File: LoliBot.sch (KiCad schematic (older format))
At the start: 25 parts, among them J1 LOLINBATT, J2 APA106, J3 SERVO1, J4 RIGHT, J5 LEFT, J6 MPU-9250, J7 APA106, SW1 SPST, U1 LOLIN32-LITE, U2 RT9276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

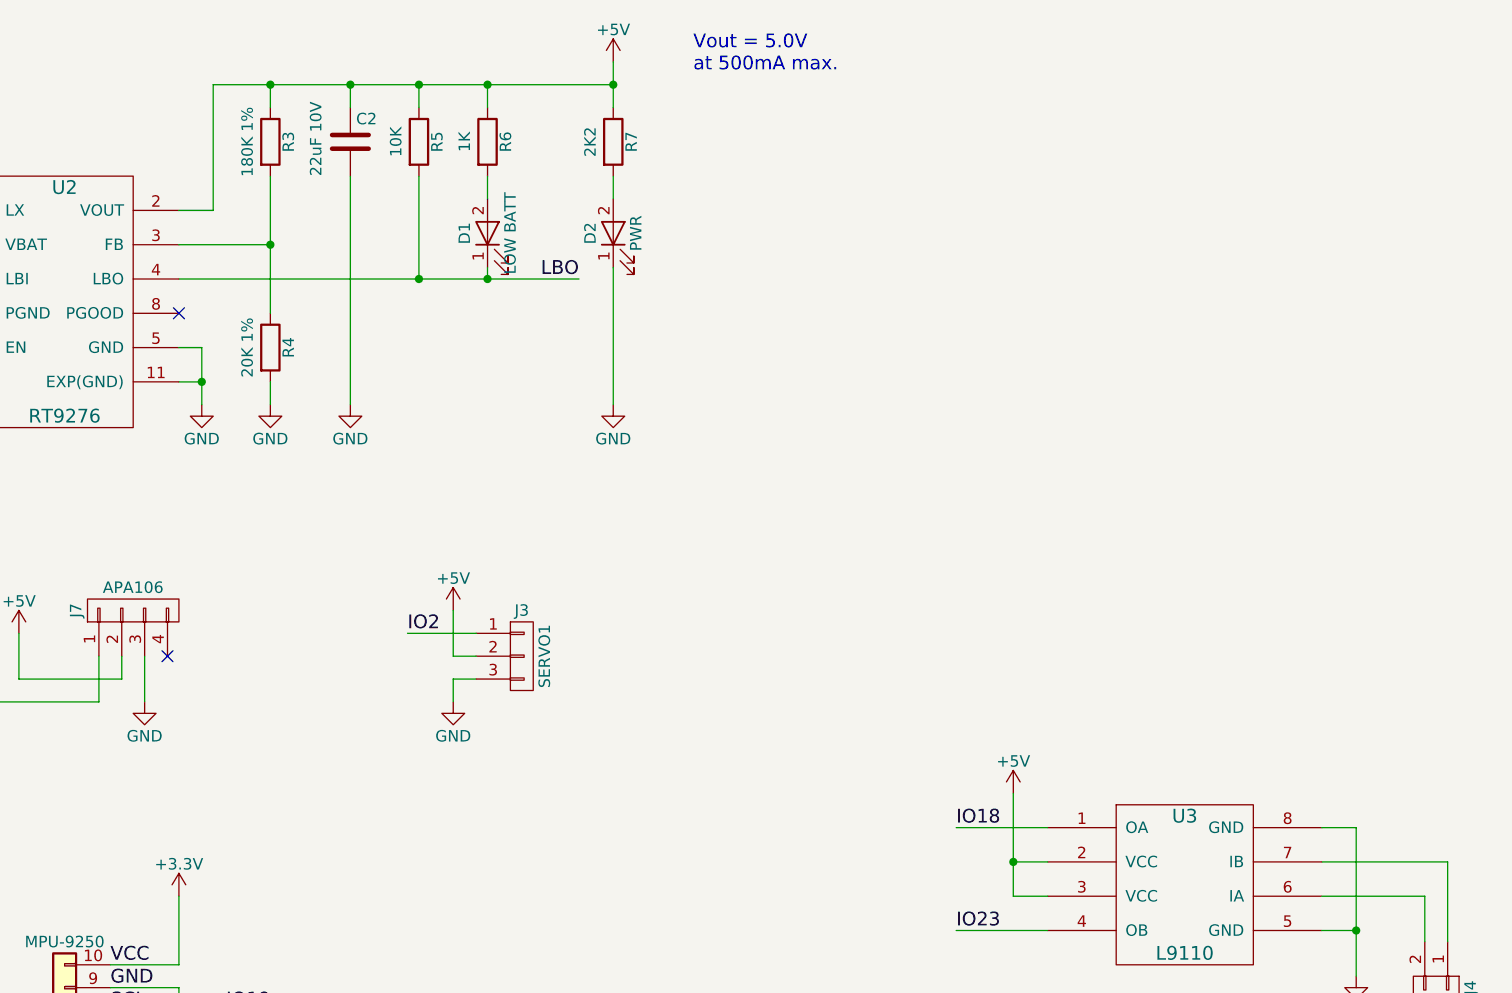
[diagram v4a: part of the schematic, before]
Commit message: Added Board for JS Version
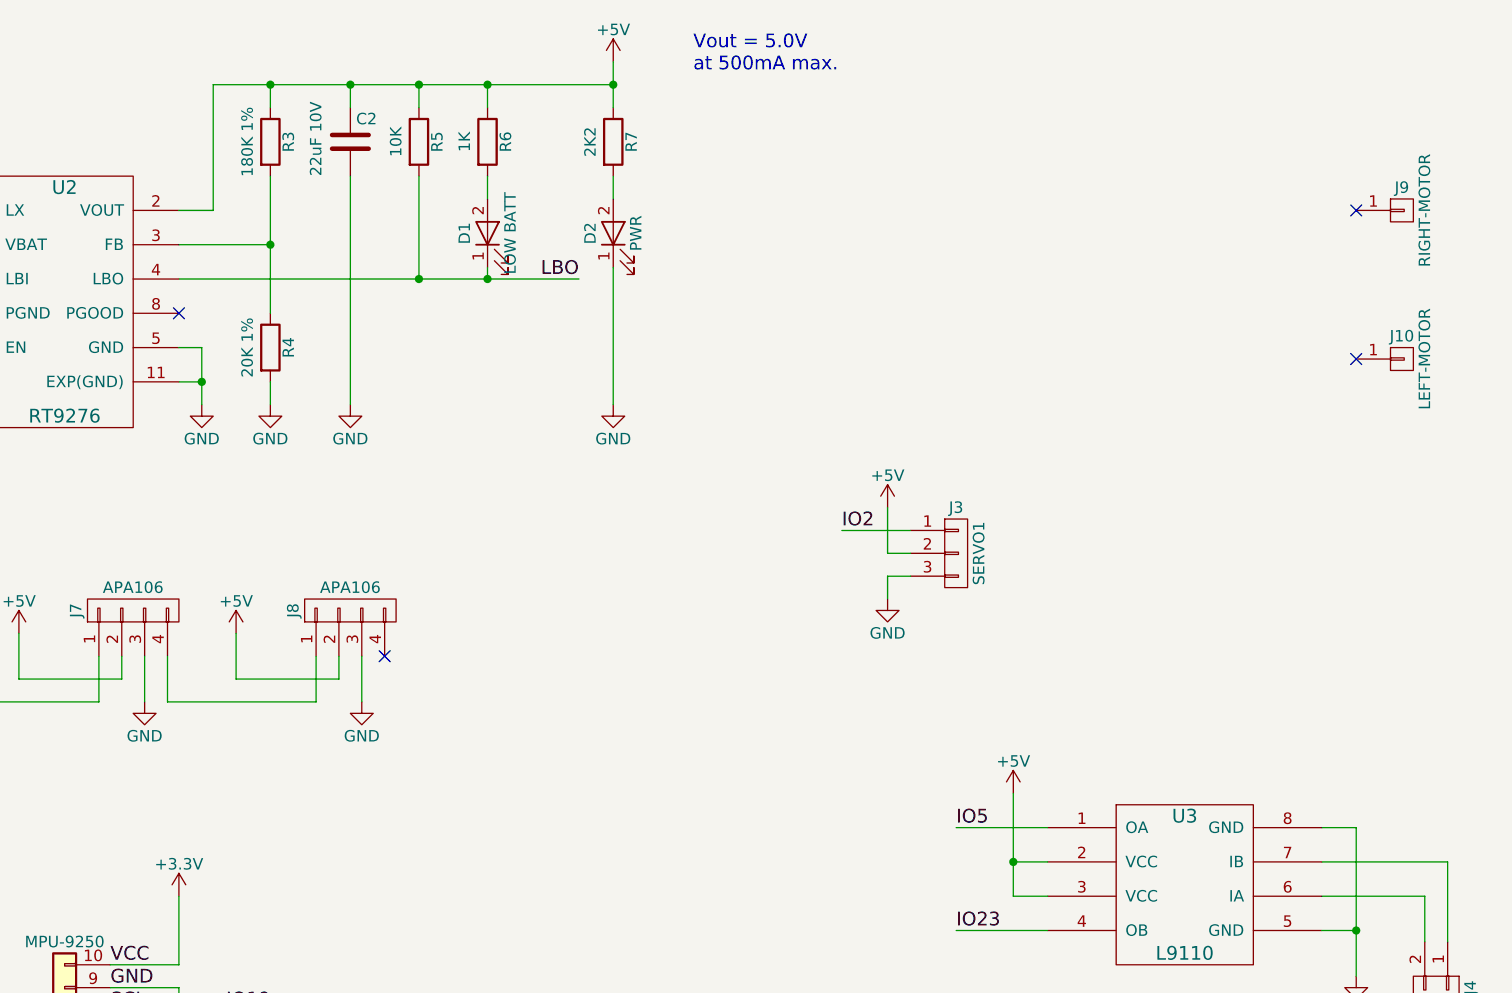
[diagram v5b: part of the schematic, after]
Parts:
- added J10: LEFT-MOTOR, libs:DC-Motor, symbol CONN_01X01
- added J8: APA106, libs:LED_8MM_APA-106, symbol CONN_01X04
- added J9: RIGHT-MOTOR, libs:DC-Motor, symbol CONN_01X01
- BT1: footprint (none) -> libs:BH-18650
- C1, C2: footprint (none) -> Capacitors_SMD:C_1210_HandSoldering
- D1, D2: footprint (none) -> LEDs:LED_D3.0mm
- J1: footprint (none) -> Pin_Headers:Pin_Header_Straight_1x02_Pitch2.54mm
- J2, J7: footprint (none) -> libs:LED_8MM_APA-106
- J3: footprint (none) -> Pin_Headers:Pin_Header_Straight_1x03_Pitch2.54mm
- J4, J5: footprint Connectors_JST:JST_PH_B2B-PH-K_02x2.00mm_Straight -> Pin_Headers:Pin_Header_Straight_1x02_Pitch2.00mm
- J6: footprint (none) -> Pin_Headers:Pin_Header_Straight_1x10_Pitch2.54mm
- R1, R2, R3, R4, R5, R6, R7: footprint (none) -> Resistors_SMD:R_0805_HandSoldering
- SW1: footprint (none) -> libs:SS12D00
- U1: footprint (none) -> libs:lolin32-lite
- U3, U4: footprint (none) -> Housings_DIP:DIP-8_W7.62mm
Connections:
- net +5V: now also J8.2 (P2)
- net GND: now also J8.3 (P3)
- net IO18: no longer U3.1 (OA)
- net IO5: now also U3.1 (OA)
- net at J7.4 (P4): now also J8.1 (P1)
- no-connect marks 7 -> 9
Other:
- moved on the sheet: J3

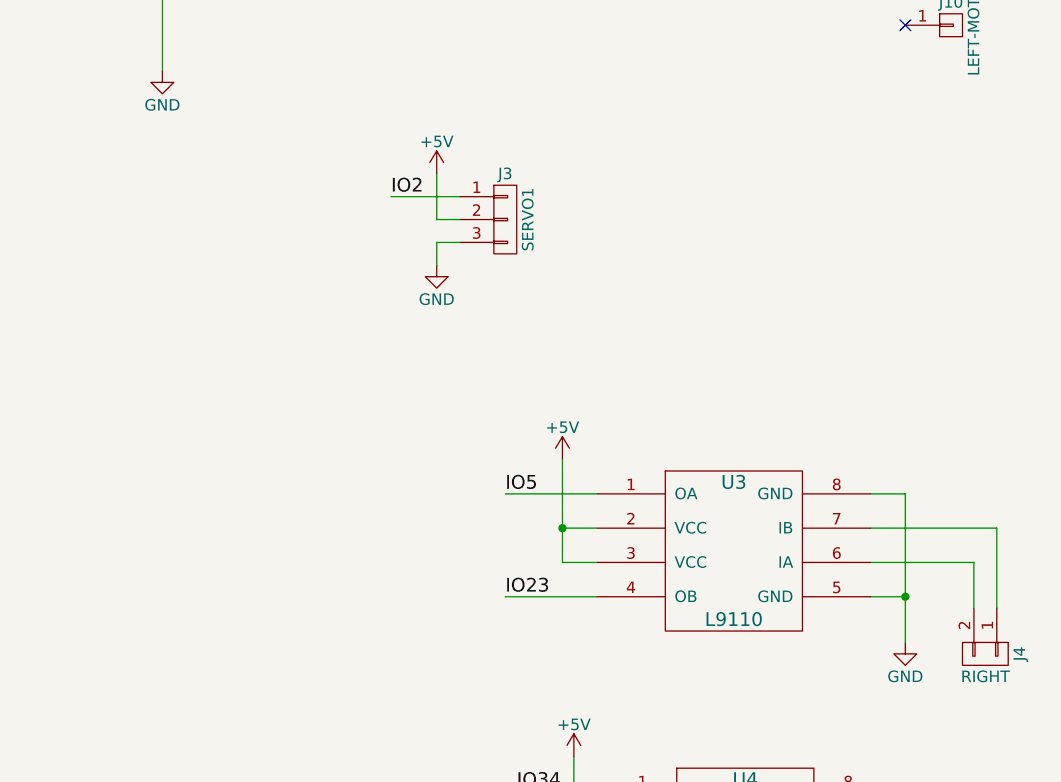
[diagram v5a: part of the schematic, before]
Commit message: Added Mounting brackets and IR sensor
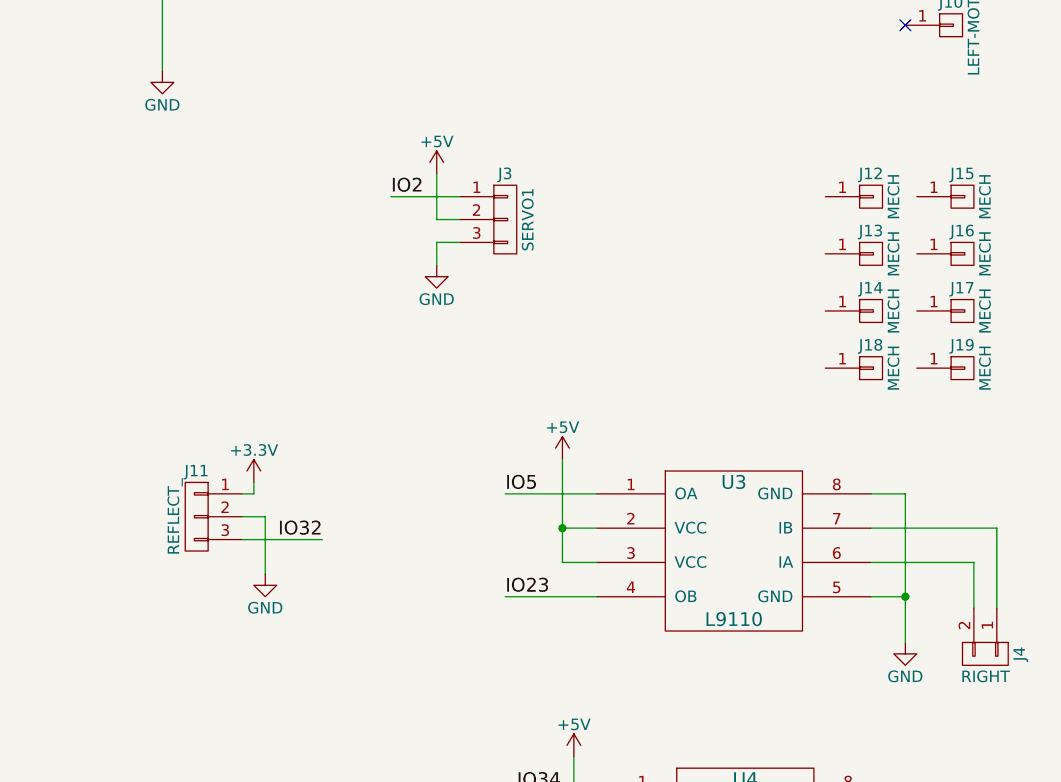
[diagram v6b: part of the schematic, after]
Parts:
- added J11: REFLECT_, Pin_Headers:Pin_Header_Straight_1x03_Pitch2.54mm, symbol CONN_01X03
- added J12, J13, J14, J15, J16, J17, J18, J19: MECH, Mounting_Holes:MountingHole_3.2mm_M3_Pad, symbol CONN_01X01
- L1: footprint (none) -> Choke_SMD:Choke_SMD_7.3x7.3_H3.5
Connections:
- net +3V3: now also J11.1 (P1)
- net GND: now also J11.2 (P2)
- net IO32: now also J11.3 (P3)
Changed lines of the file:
@@
 $EndComp
 $Comp
-L GND #PWR1
+L GND #PWR01
 U 1 1 59DB6136
 P 1250 2150
-F 0 "#PWR1" H 1250 1900 50  0001 C CNN
+F 0 "#PWR01" H 1250 1900 50  0001 C CNN
 F 1 "GND" H 1250 2000 50  0000 C CNN
 F 2 "" H 1250 2150 50  0001 C CNN
@@
 F 0 "L1" V 3350 1000 50  0000 C CNN
 F 1 "7.4uH CDRH" V 3475 1000 50  0000 C CNN
-F 2 "" H 3400 1000 50  0001 C CNN
+F 2 "Choke_SMD:Choke_SMD_7.3x7.3_H3.5" H 3400 1000 50  0001 C CNN
 F 3 "" H 3400 1000 50  0001 C CNN
 	1    3400 1000
@@
 $EndComp
 $Comp
-L GND #PWR3
+L GND #PWR02
 U 1 1 59DB694D
 P 2900 1800
-F 0 "#PWR3" H 2900 1550 50  0001 C CNN
+F 0 "#PWR02" H 2900 1550 50  0001 C CNN
 F 1 "GND" H 2900 1650 50  0000 C CNN
 F 2 "" H 2900 1800 50  0001 C CNN
@@
 	3300 2100 3300 2200
 $Comp
-L GND #PWR4
+L GND #PWR03
 U 1 1 59DB6ABB
 P 3300 2200
-F 0 "#PWR4" H 3300 1950 50  0001 C CNN
+F 0 "#PWR03" H 3300 1950 50  0001 C CNN
 F 1 "GND" H 3300 2050 50  0000 C CNN
 F 2 "" H 3300 2200 50  0001 C CNN
@@
 NoConn ~ 5300 1850
 $Comp
-L GND #PWR13
+L GND #PWR04
 U 1 1 59DB708D
 P 5400 2250
-F 0 "#PWR13" H 5400 2000 50  0001 C CNN
+F 0 "#PWR04" H 5400 2000 50  0001 C CNN
 F 1 "GND" H 5400 2100 50  0000 C CNN
 F 2 "" H 5400 2250 50  0001 C CNN
@@
 $EndComp
 $Comp
-L GND #PWR7
+L GND #PWR05
 U 1 1 59DB70B0
 P 4150 2150
-F 0 "#PWR7" H 4150 1900 50  0001 C CNN
+F 0 "#PWR05" H 4150 1900 50  0001 C CNN
 F 1 "GND" H 4150 2000 50  0000 C CNN
 F 2 "" H 4150 2150 50  0001 C CNN
@@
 Connection ~ 5700 1550
 $Comp
-L GND #PWR15
+L GND #PWR06
 U 1 1 59DB7D00
 P 5700 2250
-F 0 "#PWR15" H 5700 2000 50  0001 C CNN
+F 0 "#PWR06" H 5700 2000 50  0001 C CNN
 F 1 "GND" H 5700 2100 50  0000 C CNN
 F 2 "" H 5700 2250 50  0001 C CNN
@@
 	6050 1250 6050 2250
 $Comp
-L GND #PWR16
+L GND #PWR07
 U 1 1 59DB7E46
 P 6050 2250
-F 0 "#PWR16" H 6050 2000 50  0001 C CNN
+F 0 "#PWR07" H 6050 2000 50  0001 C CNN
 F 1 "GND" H 6050 2100 50  0000 C CNN
 F 2 "" H 6050 2250 50  0001 C CNN
@@
 $EndComp
 $Comp
-L GND #PWR19
+L GND #PWR08
 U 1 1 59DB834E
 P 7200 2250
-F 0 "#PWR19" H 7200 2000 50  0001 C CNN
+F 0 "#PWR08" H 7200 2000 50  0001 C CNN
 F 1 "GND" H 7200 2100 50  0000 C CNN
 F 2 "" H 7200 2250 50  0001 C CNN
@@
 	7200 1650 7200 2250
 $Comp
-L +5V #PWR18
+L +5V #PWR09
 U 1 1 59DB92E1
 P 7200 750
-F 0 "#PWR18" H 7200 600 50  0001 C CNN
+F 0 "#PWR09" H 7200 600 50  0001 C CNN
 F 1 "+5V" H 7200 890 50  0000 C CNN
 F 2 "" H 7200 750 50  0001 C CNN
@@
 $EndComp
 $Comp
-L +5V #PWR6
+L +5V #PWR010
 U 1 1 59DBA2B8
 P 3750 3250
-F 0 "#PWR6" H 3750 3100 50  0001 C CNN
+F 0 "#PWR010" H 3750 3100 50  0001 C CNN
 F 1 "+5V" H 3750 3390 50  0000 C CNN
 F 2 "" H 3750 3250 50  0001 C CNN
@@
 $EndComp
 $Comp
-L GND #PWR8
+L GND #PWR011
 U 1 1 59DBA675
 P 4300 3550
-F 0 "#PWR8" H 4300 3300 50  0001 C CNN
+F 0 "#PWR011" H 4300 3300 50  0001 C CNN
 F 1 "GND" H 4300 3400 50  0000 C CNN
 F 2 "" H 4300 3550 50  0001 C CNN
@@
 $EndComp
 $Comp
-L GND #PWR24
+L GND #PWR012
 U 1 1 59DBB61B
 P 10450 4750
-F 0 "#PWR24" H 10450 4500 50  0001 C CNN
+F 0 "#PWR012" H 10450 4500 50  0001 C CNN
 F 1 "GND" H 10450 4600 50  0000 C CNN
 F 2 "" H 10450 4750 50  0001 C CNN
@@
 	10850 4250 10850 4600
 $Comp
-L +5V #PWR22
+L +5V #PWR013
 U 1 1 59DBBC2C
 P 8950 3950
-F 0 "#PWR22" H 8950 3800 50  0001 C CNN
+F 0 "#PWR013" H 8950 3800 50  0001 C CNN
 F 1 "+5V" H 8950 4090 50  0000 C CNN
 F 2 "" H 8950 3950 50  0001 C CNN
@@
 $EndComp
 $Comp
-L GND #PWR25
+L GND #PWR014
 U 1 1 59DBCDC3
 P 10500 6050
-F 0 "#PWR25" H 10500 5800 50  0001 C CNN
+F 0 "#PWR014" H 10500 5800 50  0001 C CNN
 F 1 "GND" H 10500 5900 50  0000 C CNN
 F 2 "" H 10500 6050 50  0001 C CNN
@@
 	10900 5550 10900 5900
 $Comp
-L +5V #PWR23
+L +5V #PWR015
 U 1 1 59DBCDD1
 P 9000 5250
-F 0 "#PWR23" H 9000 5100 50  0001 C CNN
+F 0 "#PWR015" H 9000 5100 50  0001 C CNN
 F 1 "+5V" H 9000 5390 50  0000 C CNN
 F 2 "" H 9000 5250 50  0001 C CNN
@@
 $EndComp
 $Comp
-L +5V #PWR20
+L +5V #PWR016
 U 1 1 59DBDAEB
 P 8400 2700
-F 0 "#PWR20" H 8400 2550 50  0001 C CNN
+F 0 "#PWR016" H 8400 2550 50  0001 C CNN
 F 1 "+5V" H 8400 2840 50  0000 C CNN
 F 2 "" H 8400 2700 50  0001 C CNN
@@
 $EndComp
 $Comp
-L GND #PWR21
+L GND #PWR017
 U 1 1 59DBDB38
 P 8400 3100
-F 0 "#PWR21" H 8400 2850 50  0001 C CNN
+F 0 "#PWR017" H 8400 2850 50  0001 C CNN
 F 1 "GND" H 8400 2950 50  0000 C CNN
 F 2 "" H 8400 3100 50  0001 C CNN
@@
 IO13
 $Comp
-L +3.3V #PWR5
+L +3.3V #PWR018
 U 1 1 59DC0699
 P 3300 4450
-F 0 "#PWR5" H 3300 4300 50  0001 C CNN
+F 0 "#PWR018" H 3300 4300 50  0001 C CNN
 F 1 "+3.3V" H 3300 4590 50  0000 C CNN
 F 2 "" H 3300 4450 50  0001 C CNN
@@
 $EndComp
 $Comp
-L GND #PWR2
+L GND #PWR019
 U 1 1 59DC0B2B
 P 1300 6000
-F 0 "#PWR2" H 1300 5750 50  0001 C CNN
+F 0 "#PWR019" H 1300 5750 50  0001 C CNN
 F 1 "GND" H 1300 5850 50  0000 C CNN
 F 2 "" H 1300 6000 50  0001 C CNN
@@
 FSYNC
 $Comp
-L +3.3V #PWR11
+L +3.3V #PWR020
 U 1 1 59E28F97
 P 5300 4400
-F 0 "#PWR11" H 5300 4250 50  0001 C CNN
+F 0 "#PWR020" H 5300 4250 50  0001 C CNN
 F 1 "+3.3V" H 5300 4540 50  0000 C CNN
 F 2 "" H 5300 4400 50  0001 C CNN
@@
 	5300 4700 5300 4400
 $Comp
-L GND #PWR12
+L GND #PWR021
 U 1 1 59E29073
 P 5300 5700
-F 0 "#PWR12" H 5300 5450 50  0001 C CNN
+F 0 "#PWR021" H 5300 5450 50  0001 C CNN
 F 1 "GND" H 5300 5550 50  0000 C CNN
 F 2 "" H 5300 5700 50  0001 C CNN
@@
 IO17
 $Comp
-L +5V #PWR9
+L +5V #PWR022
 U 1 1 59E30CAE
 P 4600 3250
-F 0 "#PWR9" H 4600 3100 50  0001 C CNN
+F 0 "#PWR022" H 4600 3100 50  0001 C CNN
 F 1 "+5V" H 4600 3390 50  0000 C CNN
 F 2 "" H 4600 3250 50  0001 C CNN
@@
 	5150 3350 5150 3550
 $Comp
-L GND #PWR10
+L GND #PWR023
 U 1 1 59E30F3C
 P 5150 3550
-F 0 "#PWR10" H 5150 3300 50  0001 C CNN
+F 0 "#PWR023" H 5150 3300 50  0001 C CNN
 F 1 "GND" H 5150 3400 50  0000 C CNN
 F 2 "" H 5150 3550 50  0001 C CNN
@@
 	5900 3550 5900 3350
 $Comp
-L +5V #PWR14
+L +5V #PWR024
 U 1 1 59F090B9
 P 5550 3250
-F 0 "#PWR14" H 5550 3100 50  0001 C CNN
+F 0 "#PWR024" H 5550 3100 50  0001 C CNN
 F 1 "+5V" H 5550 3390 50  0000 C CNN
 F 2 "" H 5550 3250 50  0001 C CNN
@@
 	6100 3350 6100 3550
 $Comp
-L GND #PWR17
+L GND #PWR025
 U 1 1 59F090C3
 P 6100 3550
-F 0 "#PWR17" H 6100 3300 50  0001 C CNN
+F 0 "#PWR025" H 6100 3300 50  0001 C CNN
 F 1 "GND" H 6100 3400 50  0000 C CNN
 F 2 "" H 6100 3550 50  0001 C CNN
@@
 NoConn ~ 10450 2050
 NoConn ~ 10450 1400
+$Comp
+L CONN_01X01 J15
+U 1 1 59F9BFEA
+P 10700 2800
+F 0 "J15" H 10700 2900 50  0000 C CNN
+F 1 "MECH" V 10800 2800 50  0000 C CNN
+F 2 "Mounting_Holes:MountingHole_3.2mm_M3_Pad" H 10700 2800 50  0001 C CNN
+F 3 "" H 10700 2800 50  0001 C CNN
+	1    10700 2800
+	1    0    0    -1
+$EndComp
+$Comp
+L CONN_01X01 J16
+U 1 1 59F9C210
+P 10700 3050
+F 0 "J16" H 10700 3150 50  0000 C CNN
+F 1 "MECH" V 10800 3050 50  0000 C CNN
+F 2 "Mounting_Holes:MountingHole_3.2mm_M3_Pad" H 10700 3050 50  0001 C CNN
+F 3 "" H 10700 3050 50  0001 C CNN
+	1    10700 3050
+	1    0    0    -1
+$EndComp
+$Comp
+L CONN_01X01 J12
+U 1 1 59F9C63A
+P 10300 2800
+F 0 "J12" H 10300 2900 50  0000 C CNN
+F 1 "MECH" V 10400 2800 50  0000 C CNN
+F 2 "Mounting_Holes:MountingHole_3.2mm_M3_Pad" H 10300 2800 50  0001 C CNN
+F 3 "" H 10300 2800 50  0001 C CNN
+	1    10300 2800
+	1    0    0    -1
+$EndComp
+$Comp
+L CONN_01X01 J13
+U 1 1 59F9C640
+P 10300 3050
+F 0 "J13" H 10300 3150 50  0000 C CNN
+F 1 "MECH" V 10400 3050 50  0000 C CNN
+F 2 "Mounting_Holes:MountingHole_3.2mm_M3_Pad" H 10300 3050 50  0001 C CNN
+F 3 "" H 10300 3050 50  0001 C CNN
+	1    10300 3050
+	1    0    0    -1
+$EndComp
+$Comp
+L CONN_01X01 J17
+U 1 1 59F9C6E4
+P 10700 3300
+F 0 "J17" H 10700 3400 50  0000 C CNN
+F 1 "MECH" V 10800 3300 50  0000 C CNN
+F 2 "Mounting_Holes:MountingHole_3.2mm_M3_Pad" H 10700 3300 50  0001 C CNN
+F 3 "" H 10700 3300 50  0001 C CNN
+	1    10700 3300
+	1    0    0    -1
+$EndComp
+$Comp
+L CONN_01X01 J14
+U 1 1 59F9C6EA
+P 10300 3300
+F 0 "J14" H 10300 3400 50  0000 C CNN
+F 1 "MECH" V 10400 3300 50  0000 C CNN
+F 2 "Mounting_Holes:MountingHole_3.2mm_M3_Pad" H 10300 3300 50  0001 C CNN
+F 3 "" H 10300 3300 50  0001 C CNN
+	1    10300 3300
+	1    0    0    -1
+$EndComp
+$Comp
+L CONN_01X03 J11
+U 1 1 59F9CFA7
+P 7350 4200
+F 0 "J11" H 7350 4400 50  0000 C CNN
+F 1 "REFLECT_" V 7450 4200 50  0000 C CNN
+F 2 "Pin_Headers:Pin_Header_Straight_1x03_Pitch2.54mm" H 7350 4200 50  0001 C CNN
+F 3 "" H 7350 4200 50  0001 C CNN
+	1    7350 4200
+	-1   0    0    -1
+$EndComp
+$Comp
+L +3.3V #PWR026
+U 1 1 59F9D53B
+P 7600 4050
+F 0 "#PWR026" H 7600 3900 50  0001 C CNN
+F 1 "+3.3V" H 7600 4190 50  0000 C CNN
+F 2 "" H 7600 4050 50  0001 C CNN
+F 3 "" H 7600 4050 50  0001 C CNN
+	1    7600 4050
+	1    0    0    -1
+$EndComp
+$Comp
+L GND #PWR027
+U 1 1 59F9DB04
+P 7650 4450
+F 0 "#PWR027" H 7650 4200 50  0001 C CNN
+F 1 "GND" H 7650 4300 50  0000 C CNN
+F 2 "" H 7650 4450 50  0001 C CNN
+F 3 "" H 7650 4450 50  0001 C CNN
+	1    7650 4450
+	1    0    0    -1
+$EndComp
+Wire Wire Line
+	7550 4100 7600 4100
+Wire Wire Line
+	7600 4100 7600 4050
+Wire Wire Line
+	7550 4200 7650 4200
+Wire Wire Line
+	7650 4200 7650 4450
+Text Label 7900 4300 2    60   ~ 0
+IO32
+Wire Wire Line
+	7550 4300 7900 4300
+$Comp
+L CONN_01X01 J19
+U 1 1 59F9F795
+P 10700 3550
+F 0 "J19" H 10700 3650 50  0000 C CNN
+F 1 "MECH" V 10800 3550 50  0000 C CNN
+F 2 "Mounting_Holes:MountingHole_3.2mm_M3_Pad" H 10700 3550 50  0001 C CNN
+F 3 "" H 10700 3550 50  0001 C CNN
+	1    10700 3550
+	1    0    0    -1
+$EndComp
+$Comp
+L CONN_01X01 J18
+U 1 1 59F9F79B
+P 10300 3550
+F 0 "J18" H 10300 3650 50  0000 C CNN
+F 1 "MECH" V 10400 3550 50  0000 C CNN
+F 2 "Mounting_Holes:MountingHole_3.2mm_M3_Pad" H 10300 3550 50  0001 C CNN
+F 3 "" H 10300 3550 50  0001 C CNN
+	1    10300 3550
+	1    0    0    -1
+$EndComp
 $EndSCHEMATC

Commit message: Updated footprint
Improved motor driver positions.
Rotated acel to match x/y directions
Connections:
- net IO34: now also U4.4 (OB); no longer U4.1 (OA)
- net IO35: now also U4.1 (OA); no longer U4.4 (OB)
- net at U4.6 (IA): now also J5.1 (P1); no longer J5.2 (P2)
- net at U4.7 (IB): now also J5.2 (P2); no longer J5.1 (P1)
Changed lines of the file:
@@
 F 3 "" H 10850 6100 50  0001 C CNN
 	1    10850 6100
-	0    1    1    0
+	0    -1   1    0
 $EndComp
 $Comp
@@
 Wire Wire Line
 	9150 5850 8750 5850
+Text Label 8750 5850 0    60   ~ 0
+IO34
 Text Label 8750 5400 0    60   ~ 0
-IO34
-Text Label 8750 5850 0    60   ~ 0
 IO35
 $Comp
